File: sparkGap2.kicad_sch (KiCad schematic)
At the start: 43 parts, among them J1 9V, J2 IN, J3 OUT, Q1 BS170, SW2 pp, U1 TL072

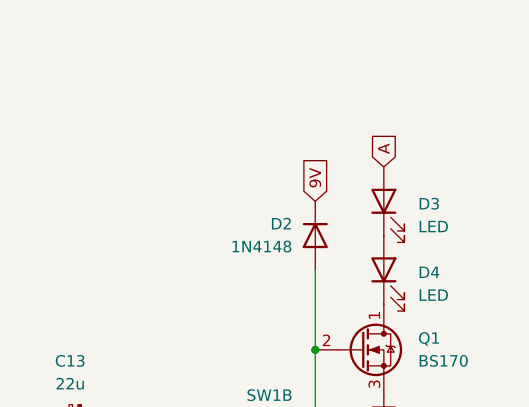
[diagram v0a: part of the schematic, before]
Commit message: Add missing current limit resistor
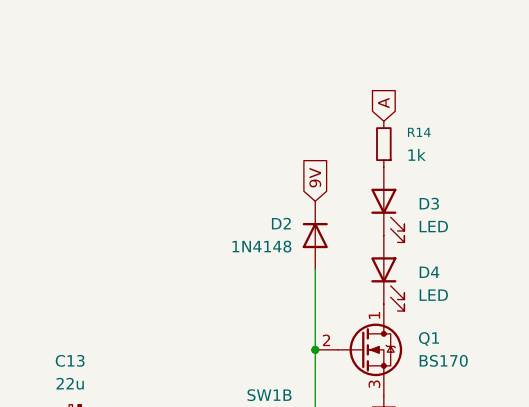
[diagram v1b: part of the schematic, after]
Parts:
- added R14: 1k, Resistor_THT:R_Axial_DIN0207_L6.3mm_D2.5mm_P7.62mm_Horizontal, symbol Device:R_Small
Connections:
- net A: now also R14.2; no longer D3.2 (A)
- new net: D3.2 (A), R14.1
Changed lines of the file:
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@@
 	(global_label "A"
 		(shape input)
-		(at 250.19 78.74 90)
+		(at 250.19 73.66 90)
 		(fields_autoplaced yes)
 		(effects
@@
 		)
 		(property "Intersheetrefs" "${INTERSHEET_REFS}"
-			(at 250.19 74.6662 90)
+			(at 250.19 69.5862 90)
 			(effects
 				(font
@@
 					(unit 1)
 				)
+			)
+		)
+	)
+	(symbol
+		(lib_id "Device:R_Small")
+		(at 250.19 76.2 180)
+		(unit 1)
+		(exclude_from_sim no)
+		(in_bom yes)
+		(on_board yes)
+		(dnp no)
+		(fields_autoplaced yes)
+		(property "Reference" "R14"
+			(at 252.73 74.9299 0)
+			(effects
+				(font
+					(size 1.016 1.016)
+				)
+				(justify right)
+			)
+		)
+		(property "Value" "1k"
+			(at 252.73 77.4699 0)
+			(effects
+				(font
+					(size 1.27 1.27)
+				)
+				(justify right)
+			)
+		)
+		(property "Footprint" "Resistor_THT:R_Axial_DIN0207_L6.3mm_D2.5mm_P7.62mm_Horizontal"
+			(at 250.19 76.2 0)
+			(effects
+				(font
+					(size 1.27 1.27)
+				)
+				(hide yes)
+			)
+		)
+		(property "Datasheet" "~"
+			(at 250.19 76.2 0)
+			(effects
+				(font
+					(size 1.27 1.27)
+				)
+				(hide yes)
+			)
+		)
+		(property "Description" "Resistor, small symbol"
+			(at 250.19 76.2 0)
+			(effects
+				(font
+					(size 1.27 1.27)
+				)
+				(hide yes)
+			)
+		)
+		(pin "2"
+		)
+		(pin "1"
+		)
+		(instances
+			(project "sparkGap2"
+				(path "/bd6cf20e-4683-4745-aaa3-17469f6777ac"
+					(reference "R14")
+					(unit 1)
+				)

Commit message: Improve gnd routing and gfx
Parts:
- Q1: footprint Package_TO_SOT_THT:TO-92_Inline -> Package_TO_SOT_THT:TO-92_Inline_Wide
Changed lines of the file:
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@@
 			)
 		)
-		(property "Footprint" "Package_TO_SOT_THT:TO-92_Inline"
+		(property "Footprint" "Package_TO_SOT_THT:TO-92_Inline_Wide"
 			(at 252.73 100.965 0)
 			(effects

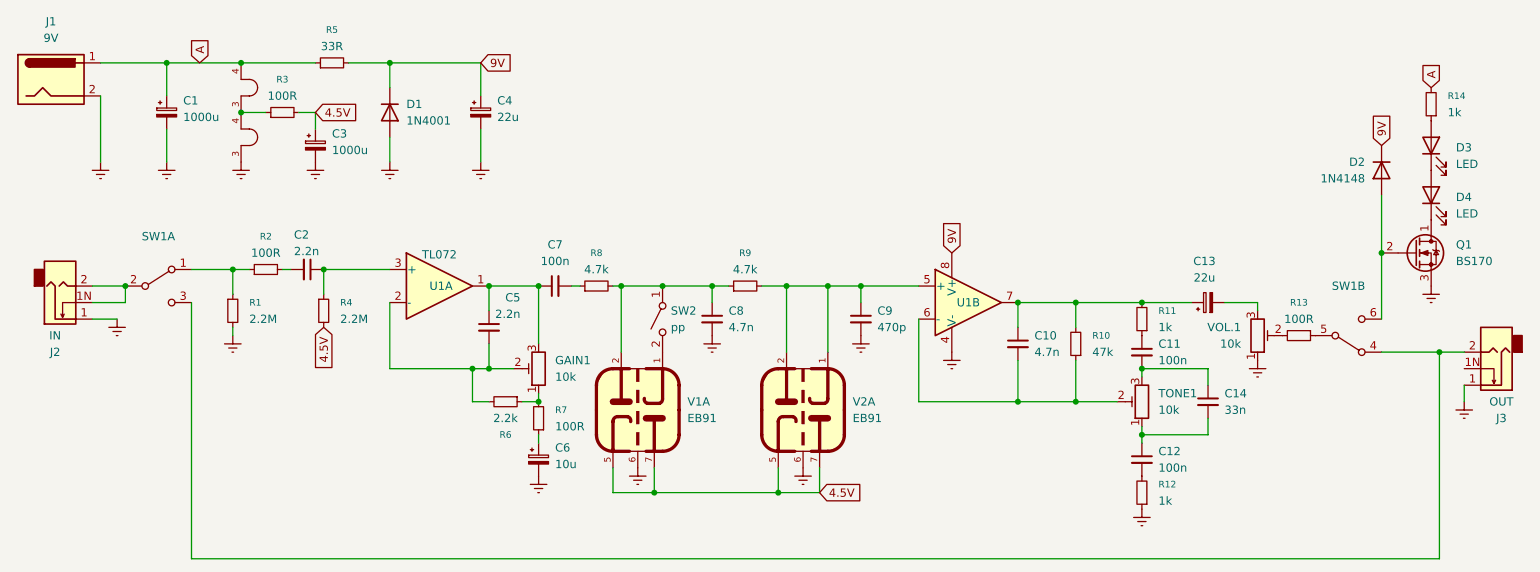
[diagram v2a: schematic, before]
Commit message: Fix schematic errors. Renumber to match ValveWizard schematic. Improve layout. Switch to 4 layer
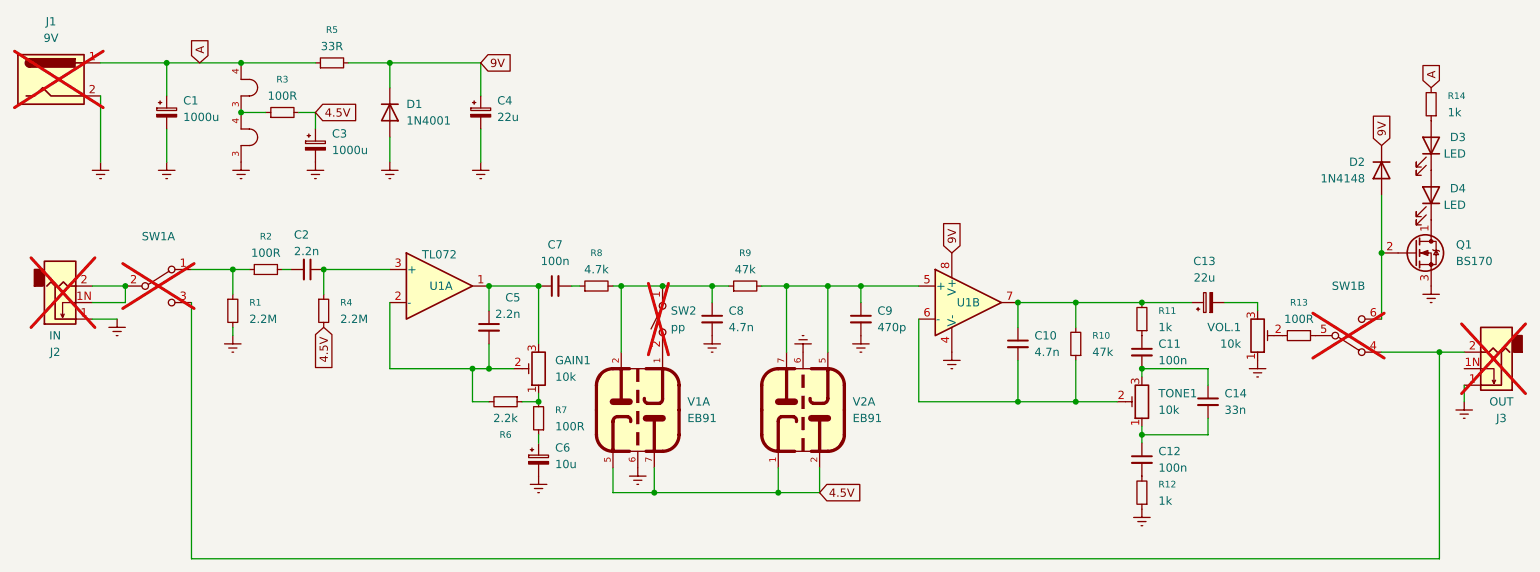
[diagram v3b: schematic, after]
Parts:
- D1: footprint Diode_THT:D_DO-41_SOD81_P5.08mm_Vertical_AnodeUp -> Diode_THT:D_DO-41_SOD81_P2.54mm_Vertical_AnodeUp
- D2: footprint Diode_THT:D_DO-35_SOD27_P5.08mm_Vertical_AnodeUp -> Diode_THT:D_DO-35_SOD27_P2.54mm_Vertical_AnodeUp
- J1, J2, J3, SW1, SW2: now not fitted
- R1, R10, R11, R12, R13, R14, R2, R3, R4, R5, R6, R7, R8: footprint Resistor_THT:R_Axial_DIN0207_L6.3mm_D2.5mm_P7.62mm_Horizontal -> Resistor_THT:R_Axial_DIN0207_L6.3mm_D2.5mm_P2.54mm_Vertical
- R9: value 4.7k -> 47k
- V1, V2: footprint Valves_complete:B7G (7 Pin Mini) Dual Use -> Valves_complete:B7G (7 Pin Mini)-B9A-shield-mount
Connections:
- net 4.5V: now also V2.1, V2.2; no longer V2.5, V2.7
- net at C9.1, R9.2, U1.5 (+): now also V2.5, V2.7; no longer V2.1, V2.2
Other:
- moved on the sheet: D3, D4
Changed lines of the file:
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@@
 		(in_bom yes)
 		(on_board yes)
-		(dnp no)
+		(dnp yes)
 		(property "Reference" "J2"
 			(at 38.735 114.3 0)
@@
 			)
 		)
-		(property "Footprint" "Resistor_THT:R_Axial_DIN0207_L6.3mm_D2.5mm_P7.62mm_Horizontal"
+		(property "Footprint" "Resistor_THT:R_Axial_DIN0207_L6.3mm_D2.5mm_P2.54mm_Vertical"
 			(at 81.28 69.85 0)
 			(effects
@@
 	)
 	(symbol
+		(lib_id "RCA_Valve:EB91")
+		(at 153.67 123.19 180)
+		(unit 1)
+		(exclude_from_sim no)
+		(in_bom yes)
+		(on_board yes)
+		(dnp no)
+		(fields_autoplaced yes)
+		(property "Reference" "V2"
+			(at 161.29 121.9199 0)
+			(effects
+				(font
+					(size 1.27 1.27)
+				)
+				(justify right)
+			)
+		)
+		(property "Value" "EB91"
+			(at 161.29 124.4599 0)
+			(effects
+				(font
+					(size 1.27 1.27)
+				)
+				(justify right)
+			)
+		)
+		(property "Footprint" "Valves_complete:B7G (7 Pin Mini)-B9A-shield-mount"
+			(at 153.67 123.19 0)
+			(effects
+				(font
+					(size 1.27 1.27)
+				)
+				(hide yes)
+			)
+		)
+		(property "Datasheet" ""
+			(at 153.67 123.19 0)
+			(effects
+				(font
+					(size 1.27 1.27)
+				)
+				(hide yes)
+			)
+		)
+		(property "Description" ""
+			(at 153.67 123.19 0)
+			(effects
+				(font
+					(size 1.27 1.27)
+				)
+				(hide yes)
+			)
+		)
+		(pin "7"
+		)
+		(pin "4"
+		)
+		(pin "1"
+		)
+		(pin "3"
+		)
+		(pin "6"
+		)
+		(pin "5"
+		)
+		(pin "2"
+		)
+		(instances
+			(project "sparkGap2"
+				(path "/bd6cf20e-4683-4745-aaa3-17469f6777ac"
+					(reference "V2")
+					(unit 1)
+				)
+			)
+		)
+	)
+	(symbol
 		(lib_id "Device:R_Small")
 		(at 107.95 121.92 270)
@@
 			)
 		)
-		(property "Footprint" "Resistor_THT:R_Axial_DIN0207_L6.3mm_D2.5mm_P7.62mm_Horizontal"
+		(property "Footprint" "Resistor_THT:R_Axial_DIN0207_L6.3mm_D2.5mm_P2.54mm_Vertical"
 			(at 107.95 121.92 0)
 			(effects
@@
 			)
 		)
-		(property "Footprint" "Diode_THT:D_DO-41_SOD81_P5.08mm_Vertical_AnodeUp"
+		(property "Footprint" "Diode_THT:D_DO-41_SOD81_P2.54mm_Vertical_AnodeUp"
 			(at 90.17 77.47 0)
 			(effects
@@
 	)
 	(symbol
-		(lib_id "RCA_Valve:EB91")
-		(at 153.67 123.19 0)
-		(unit 1)
-		(exclude_from_sim no)
-		(in_bom yes)
-		(on_board yes)
-		(dnp no)
-		(fields_autoplaced yes)
-		(property "Reference" "V2"
-			(at 161.29 121.9199 0)
-			(effects
-				(font
-					(size 1.27 1.27)
-				)
-				(justify left)
-			)
-		)
-		(property "Value" "EB91"
-			(at 161.29 124.4599 0)
-			(effects
-				(font
-					(size 1.27 1.27)
-				)
-				(justify left)
-			)
-		)
-		(property "Footprint" "Valves_complete:B7G (7 Pin Mini) Dual Use"
-			(at 153.67 123.19 0)
-			(effects
-				(font
-					(size 1.27 1.27)
-				)
-				(hide yes)
-			)
-		)
-		(property "Datasheet" ""
-			(at 153.67 123.19 0)
-			(effects
-				(font
-					(size 1.27 1.27)
-				)
-				(hide yes)
-			)
-		)
-		(property "Description" ""
-			(at 153.67 123.19 0)
-			(effects
-				(font
-					(size 1.27 1.27)
-				)
-				(hide yes)
-			)
-		)
-		(pin "7"
-		)
-		(pin "4"
-		)
-		(pin "1"
-		)
-		(pin "3"
-		)
-		(pin "6"
-		)
-		(pin "5"
-		)
-		(pin "2"
-		)
-		(instances
-			(project ""
-				(path "/bd6cf20e-4683-4745-aaa3-17469f6777ac"
-					(reference "V2")
-					(unit 1)
-				)
-			)
-		)
-	)
-	(symbol
 		(lib_id "power:Earth")
 		(at 55.88 85.09 0)
@@
 			)
 		)
-		(property "Footprint" "Resistor_THT:R_Axial_DIN0207_L6.3mm_D2.5mm_P7.62mm_Horizontal"
+		(property "Footprint" "Resistor_THT:R_Axial_DIN0207_L6.3mm_D2.5mm_P2.54mm_Vertical"
 			(at 250.19 76.2 0)
 			(effects
@@
 		(in_bom yes)
 		(on_board yes)
-		(dnp no)
+		(dnp yes)
 		(fields_autoplaced yes)
 		(property "Reference" "J1"
@@
 			)
 		)
-		(property "Footprint" "Resistor_THT:R_Axial_DIN0207_L6.3mm_D2.5mm_P7.62mm_Horizontal"
+		(property "Footprint" "Resistor_THT:R_Axial_DIN0207_L6.3mm_D2.5mm_P2.54mm_Vertical"
 			(at 80.01 107.95 0)
 			(effects
@@
 		(in_bom yes)
 		(on_board yes)
-		(dnp no)
+		(dnp yes)
 		(fields_autoplaced yes)
 		(property "Reference" "SW1"
@@
 	(symbol
 		(lib_id "Device:LED")
-		(at 250.19 82.55 90)
+		(at 250.19 82.55 270)
+		(mirror x)
 		(unit 1)
 		(exclude_from_sim no)
@@
 		(on_board yes)
 		(dnp no)
-		(fields_autoplaced yes)
 		(property "Reference" "D3"
-			(at 254 82.8674 90)
+			(at 255.524 81.28 90)
 			(effects
 				(font
@@
 		)
 		(property "Value" "LED"
-			(at 254 85.4074 90)
+			(at 255.524 83.82 90)
 			(effects
 				(font
@@
 			)
 		)
-		(property "Footprint" "Resistor_THT:R_Axial_DIN0207_L6.3mm_D2.5mm_P7.62mm_Horizontal"
+		(property "Footprint" "Resistor_THT:R_Axial_DIN0207_L6.3mm_D2.5mm_P2.54mm_Vertical"
 			(at 66.04 107.95 0)
 			(effects
@@
 			)
 		)
-		(property "Footprint" "Resistor_THT:R_Axial_DIN0207_L6.3mm_D2.5mm_P7.62mm_Horizontal"
+		(property "Footprint" "Resistor_THT:R_Axial_DIN0207_L6.3mm_D2.5mm_P2.54mm_Vertical"
 			(at 195.58 113.03 0)
 			(effects
@@
 			)
 		)
-		(property "Footprint" "Valves_complete:B7G (7 Pin Mini) Dual Use"
+		(property "Footprint" "Valves_complete:B7G (7 Pin Mini)-B9A-shield-mount"
 			(at 67.31 73.66 0)
 			(effects
@@
 		(in_bom yes)
 		(on_board yes)
-		(dnp no)
+		(dnp yes)
 		(fields_autoplaced yes)
 		(property "Reference" "SW1"
@@
 			)
 		)
-		(property "Footprint" "Diode_THT:D_DO-35_SOD27_P5.08mm_Vertical_AnodeUp"
+		(property "Footprint" "Diode_THT:D_DO-35_SOD27_P2.54mm_Vertical_AnodeUp"
 			(at 242.57 86.36 0)
 			(effects
@@
 			)
 		)
-		(property "Footprint" "Resistor_THT:R_Axial_DIN0207_L6.3mm_D2.5mm_P7.62mm_Horizontal"
+		(property "Footprint" "Resistor_THT:R_Axial_DIN0207_L6.3mm_D2.5mm_P2.54mm_Vertical"
 			(at 205.74 135.89 0)
 			(effects
@@
 			)
 		)
-		(property "Value" "4.7k"
+		(property "Value" "47k"
 			(at 144.78 101.6 90)
 			(effects
@@
 			)
 		)
-		(property "Footprint" "Resistor_THT:R_Axial_DIN0207_L6.3mm_D2.5mm_P7.62mm_Horizontal"
+		(property "Footprint" "Resistor_THT:R_Axial_DIN0207_L6.3mm_D2.5mm_P2.54mm_Vertical"
 			(at 113.03 124.46 0)
 			(effects
@@
 	(symbol
 		(lib_id "power:Earth")
-		(at 153.67 132.08 0)
+		(at 153.67 114.3 180)
 		(unit 1)
 		(exclude_from_sim no)
@@
 		(fields_autoplaced yes)
 		(property "Reference" "#PWR012"
-			(at 153.67 138.43 0)
+			(at 153.67 107.95 0)
 			(effects
 				(font
@@
 		)
 		(property "Value" "Earth"
-			(at 153.67 137.16 0)
+			(at 153.67 109.22 0)
 			(effects
 				(font
@@
 		)
 		(property "Footprint" ""
-			(at 153.67 132.08 0)
+			(at 153.67 114.3 0)
 			(effects
 				(font
@@
 		)
 		(property "Datasheet" "~"
-			(at 153.67 132.08 0)
+			(at 153.67 114.3 0)
 			(effects
 				(font
@@
 		)
 		(property "Description" "Power symbol creates a global label with name \"Earth\""
-			(at 153.67 132.08 0)
+			(at 153.67 114.3 0)
 			(effects
 				(font
@@
 		(in_bom yes)
 		(on_board yes)
-		(dnp no)
+		(dnp yes)
 		(fields_autoplaced yes)
 		(property "Reference" "SW2"
@@
 			)
 		)
-		(property "Footprint" "Resistor_THT:R_Axial_DIN0207_L6.3mm_D2.5mm_P7.62mm_Horizontal"
+		(property "Footprint" "Resistor_THT:R_Axial_DIN0207_L6.3mm_D2.5mm_P2.54mm_Vertical"
 			(at 229.87 111.76 0)
 			(effects
@@
 			)
 		)
-		(property "Footprint" "Resistor_THT:R_Axial_DIN0207_L6.3mm_D2.5mm_P7.62mm_Horizontal"
+		(property "Footprint" "Resistor_THT:R_Axial_DIN0207_L6.3mm_D2.5mm_P2.54mm_Vertical"
 			(at 205.74 109.22 0)
 			(effects
@@
 			)
 		)
-		(property "Footprint" "Resistor_THT:R_Axial_DIN0207_L6.3mm_D2.5mm_P7.62mm_Horizontal"
+		(property "Footprint" "Resistor_THT:R_Axial_DIN0207_L6.3mm_D2.5mm_P2.54mm_Vertical"
 			(at 71.12 101.6 0)
 			(effects
@@
 			)
 		)
-		(property "Footprint" "Resistor_THT:R_Axial_DIN0207_L6.3mm_D2.5mm_P7.62mm_Horizontal"
+		(property "Footprint" "Resistor_THT:R_Axial_DIN0207_L6.3mm_D2.5mm_P2.54mm_Vertical"
 			(at 73.66 77.47 0)
 			(effects
@@
 	(symbol
 		(lib_id "Device:LED")
-		(at 250.19 90.17 90)
+		(at 250.19 90.17 270)
+		(mirror x)
 		(unit 1)
 		(exclude_from_sim no)
@@
 		(on_board yes)
 		(dnp no)
-		(fields_autoplaced yes)
 		(property "Reference" "D4"
-			(at 254 90.4874 90)
+			(at 255.524 89.154 90)
 			(effects
 				(font
@@
 		)
 		(property "Value" "LED"
-			(at 254 93.0274 90)
+			(at 255.524 91.694 90)
 			(effects
 				(font
@@
 			)
 		)
-		(property "Footprint" "Resistor_THT:R_Axial_DIN0207_L6.3mm_D2.5mm_P7.62mm_Horizontal"
+		(property "Footprint" "Resistor_THT:R_Axial_DIN0207_L6.3mm_D2.5mm_P2.54mm_Vertical"
 			(at 121.92 104.14 0)
 			(effects
@@
 		(in_bom yes)
 		(on_board yes)
-		(dnp no)
+		(dnp yes)
 		(property "Reference" "J3"
 			(at 260.985 124.46 0)
@@
 			)
 		)
-		(property "Footprint" "Valves_complete:B7G (7 Pin Mini) Dual Use"
+		(property "Footprint" "Valves_complete:B7G (7 Pin Mini)-B9A-shield-mount"
 			(at 128.27 123.19 0)
 			(effects
@@
 			)
 		)
-		(property "Footprint" "Valves_complete:B7G (7 Pin Mini) Dual Use"
+		(property "Footprint" "Valves_complete:B7G (7 Pin Mini)-B9A-shield-mount"
 			(at 67.31 81.28 0)
 			(effects
